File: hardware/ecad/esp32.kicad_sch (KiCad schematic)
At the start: 0 parts

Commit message: finsihed 6/7 sheets, usb_data needs work. Some warnings to be dealt with aswell but no hard errors.
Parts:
- added C10: 10uF, Capacitor_SMD:C_01005_0402Metric, symbol Device:C
- added C11, C12, C13, C9: 100nF, Capacitor_SMD:C_01005_0402Metric, symbol Device:C
- added J3: UART, symbol Connector:Conn_01x06_Pin
- added R10: 100, Resistor_SMD:R_0201_0603Metric, symbol Device:R
- added R7, R8, R9: 10k, Resistor_SMD:R_0201_0603Metric, symbol Device:R
- added SW1, SW2: SW_Push, Button_Switch_SMD:SW_SPST_B3U-1000P, symbol Switch:SW_Push
- added SW3: SW_SPDT, Button_Switch_THT:SW_Slide_SPDT_Angled_CK_OS102011MA1Q, symbol Switch:SW_SPDT
- added U4: ESP32-S3-WROOM-1, RF_Module:ESP32-S3-WROOM-1, symbol RF_Module:ESP32-S3-WROOM-1
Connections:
- new net: R10.2, SW3.2 (B)
- new net BAT_SENSE: U4.4 (IO4)
- new net BOOT_BUTTON: C12.1, J3.6 (Pin_6), R8.2, SW2.1, U4.27 (IO0)
- new net EN: C11.1, J3.5 (Pin_5), R7.2, SW1.1, U4.3 (EN)
- new net GND: C10.2, C11.2, C12.2, C13.1, C9.2, J3.2 (Pin_2), R9.2, SW1.2, SW2.2, U4.1 (GND), U4.40 (GND), U4.41 (GND)
- new net MODE_SEL: C13.2, R10.1, R9.1, U4.38 (IO2)
- new net OLED_CLK: U4.29 (IO36)
- new net OLED_CS: U4.17 (IO9)
- new net OLED_DC: U4.18 (IO10)
- new net OLED_MOSI: U4.28 (IO35)
- new net OLED_RES: U4.12 (IO8)
- new net RX0: J3.4 (Pin_4), U4.36 (RXD0)
- new net SYS_3V3: C10.1, C9.1, J3.1 (Pin_1), R7.1, R8.1, SW3.1 (A), U4.2 (3V3)
- new net TX0: J3.3 (Pin_3), U4.37 (TXD0)
- new net USB_D+_ESP: U4.14 (USB_D+)
- new net USB_D-_ESP: U4.13 (USB_D-)
- no-connect marks 0 -> 25
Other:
- company: (none) -> āvega systems
- title: (none) -> midi2BLE_ESP32_S3

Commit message: Updated schematics to get rid of errors and warnings
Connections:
- net EN renamed RST_BUTTON
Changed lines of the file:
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@@
-	)
-	(junction
-		(at 135.89 63.5)
-		(diameter 0)
-		(color 0 0 0 0)
-	)
-	(junction
-		(at 135.89 68.58)
-		(diameter 0)
-		(color 0 0 0 0)
 	)
 	(junction
@@
 	(wire
 		(pts
-			(xy 132.08 60.96) (xy 135.89 60.96)
+			(xy 132.08 63.5) (xy 135.89 63.5)
 		)
 		(stroke
@@
 	(wire
 		(pts
-			(xy 135.89 68.58) (xy 135.89 66.04)
-		)
-		(stroke
-			(width 0)
-			(type default)
-		)
-	)
-	(wire
-		(pts
 			(xy 208.28 20.32) (xy 215.9 20.32)
 		)
@@
 	(wire
 		(pts
-			(xy 135.89 60.96) (xy 135.89 63.5)
-		)
-		(stroke
-			(width 0)
-			(type default)
-		)
-	)
-	(wire
-		(pts
-			(xy 135.89 66.04) (xy 132.08 66.04)
+			(xy 135.89 68.58) (xy 132.08 68.58)
 		)
 		(stroke
@@
 	(wire
 		(pts
-			(xy 132.08 68.58) (xy 135.89 68.58)
-		)
-		(stroke
-			(width 0)
-			(type default)
-		)
-	)
-	(wire
-		(pts
 			(xy 142.24 166.37) (xy 138.43 166.37)
 		)
@@
 	(wire
 		(pts
-			(xy 132.08 63.5) (xy 135.89 63.5)
-		)
-		(stroke
-			(width 0)
-			(type default)
-		)
-	)
-	(wire
-		(pts
 			(xy 269.24 45.72) (xy 269.24 41.91)
 		)
@@
 		)
 	)
-	(label "IO0"
-		(at 132.08 68.58 180)
-		(effects
-			(font
-				(size 1.27 1.27)
-			)
-			(justify right bottom)
-		)
-	)
-	(label "IO0"
+	(label "BOOT_BUTTON"
 		(at 215.9 33.02 0)
 		(effects
@@
 	)
 	(label "RST_BUTTON"
-		(at 132.08 60.96 180)
+		(at 132.08 63.5 180)
 		(effects
 			(font
@@
 	)
 	(label "BOOT_BUTTON"
-		(at 132.08 66.04 180)
+		(at 132.08 68.58 180)
 		(effects
 			(font
@@
 		)
 	)
-	(label "EN"
-		(at 132.08 63.5 180)
-		(effects
-			(font
-				(size 1.27 1.27)
-			)
-			(justify right bottom)
-		)
-	)
 	(label "RX0"
 		(at 215.9 27.94 0)
@@
 		)
 	)
-	(label "EN"
+	(label "RST_BUTTON"
 		(at 215.9 30.48 0)
 		(effects

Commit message: Updated schematics and added printed pdf
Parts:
- C10: footprint Capacitor_SMD:C_01005_0402Metric -> Capacitor_SMD:C_0603_1608Metric
- C11, C12, C9: footprint Capacitor_SMD:C_01005_0402Metric -> Capacitor_SMD:C_0402_1005Metric
- R10, R7, R8, R9: footprint Resistor_SMD:R_0201_0603Metric -> Capacitor_SMD:C_0402_1005Metric
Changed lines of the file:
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@@
 			)
 		)
-		(property "Footprint" "Capacitor_SMD:C_01005_0402Metric"
+		(property "Footprint" "Capacitor_SMD:C_0402_1005Metric"
 			(at 260.35 61.2648 0)
 			(hide yes)
@@
 			)
 		)
-		(property "Footprint" "Capacitor_SMD:C_01005_0402Metric"
+		(property "Footprint" "Capacitor_SMD:C_0603_1608Metric"
 			(at 260.35 40.9448 0)
 			(hide yes)
@@
 			)
 		)
-		(property "Footprint" "Capacitor_SMD:C_01005_0402Metric"
+		(property "Footprint" "Capacitor_SMD:C_0402_1005Metric"
 			(at 260.35 101.9048 0)
 			(hide yes)
@@
 			)
 		)
-		(property "Footprint" "Resistor_SMD:R_0201_0603Metric"
+		(property "Footprint" "Capacitor_SMD:C_0402_1005Metric"
 			(at 255.27 87.122 90)
 			(hide yes)
@@
 			)
 		)
-		(property "Footprint" "Capacitor_SMD:C_01005_0402Metric"
+		(property "Footprint" "Capacitor_SMD:C_0402_1005Metric"
 			(at 260.35 28.2448 0)
 			(hide yes)
@@
 			)
 		)
-		(property "Footprint" "Resistor_SMD:R_0201_0603Metric"
+		(property "Footprint" "Capacitor_SMD:C_0402_1005Metric"
 			(at 52.07 24.638 90)
 			(hide yes)
@@
 			)
 		)
-		(property "Footprint" "Resistor_SMD:R_0201_0603Metric"
+		(property "Footprint" "Capacitor_SMD:C_0402_1005Metric"
 			(at 29.972 30.48 90)
 			(hide yes)
@@
 			)
 		)
-		(property "Footprint" "Resistor_SMD:R_0201_0603Metric"
+		(property "Footprint" "Capacitor_SMD:C_0402_1005Metric"
 			(at 255.27 127.762 90)
 			(hide yes)

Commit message: docs(hardware): update ecad README to reflect completed schematic and PCB — PCB IS DONE!!!
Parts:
- removed J3: UART, symbol Connector:Conn_01x06_Pin
- added TP1, TP2, TP3, TP4, TP5, TP6: TestPoint, symbol Connector:TestPoint
- C13: footprint Capacitor_SMD:C_01005_0402Metric -> Capacitor_SMD:C_0402_1005Metric
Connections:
- net BOOT_BUTTON: now also TP6.1
- net GND: now also TP2.1
- net RST_BUTTON: now also TP5.1
- net RX0: now also TP4.1
- net SYS_3V3: now also TP1.1
- net TX0: now also TP3.1
- net USB_D+_ESP renamed USB_ESP+
- net USB_D-_ESP renamed USB_ESP-
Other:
- note added: "UART TEST POINTS"

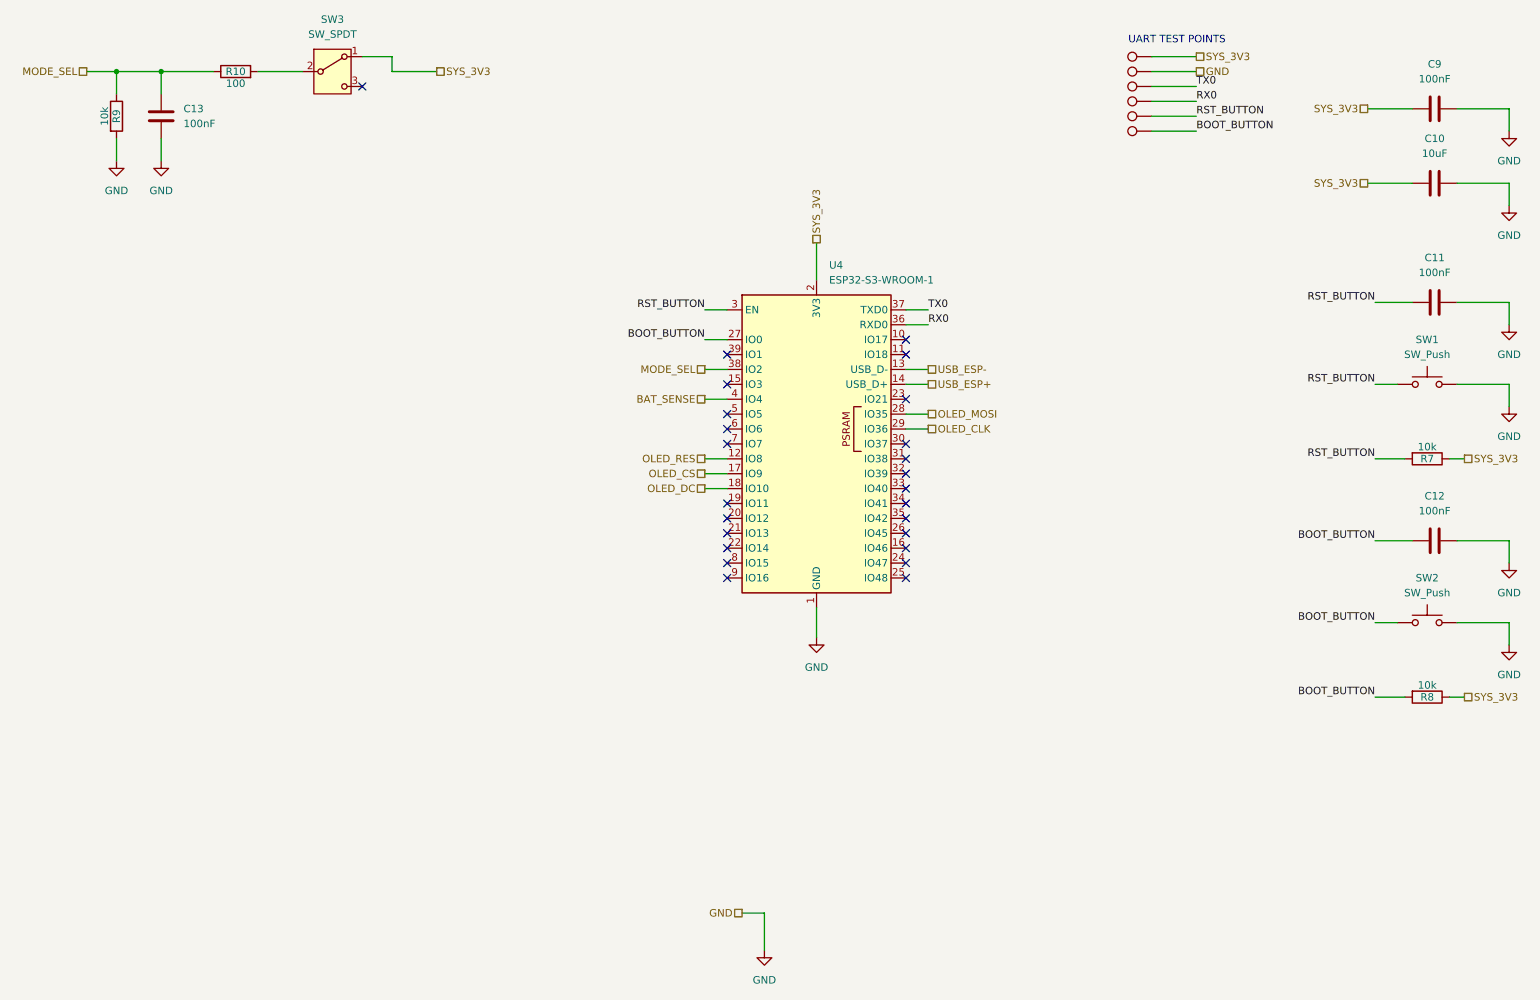
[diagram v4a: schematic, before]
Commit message: fix: resolve fatal power and USB switching errors
Replace TLV61047 boost converter with MT3608; add SS14 catch diode, 4.7µH inductor, and correct FB divider (180kΩ/51kΩ) for 5V output
Fix TPS62162DSG EN circular dependency; connect directly to U1_OUT
Fix TPS62162DSG FB pin; disconnect from SYS_3V3 and tie to GND
Fix TPS2116 power mux; remove series resistor on VIN1, add correct PR1 divider (100kΩ/27kΩ), tie MODE to VIN1 for priority mode
Fix TS3USB30E OE pin; tie directly to GND to keep switch always enabled
Add PGOOD pull-up resistor (10kΩ) to SYS_3V3 on BQ24079
Change ISET resistor from 590Ω to 680Ω for 1.3A charge current
Remove unnecessary R5 (10kΩ VBUS_IN to GND bleed resistor)
Add USB_STATUS net from TPS2116 ST pin to ESP32 IO38
Add PWR_FLAG to BOOST_5V and U1_OUT nets
Fix U1_PGOOD net label placement; separate from SYS_3V3 pull-up node
Add documentation boxes and truth tables to power and USB switching pages
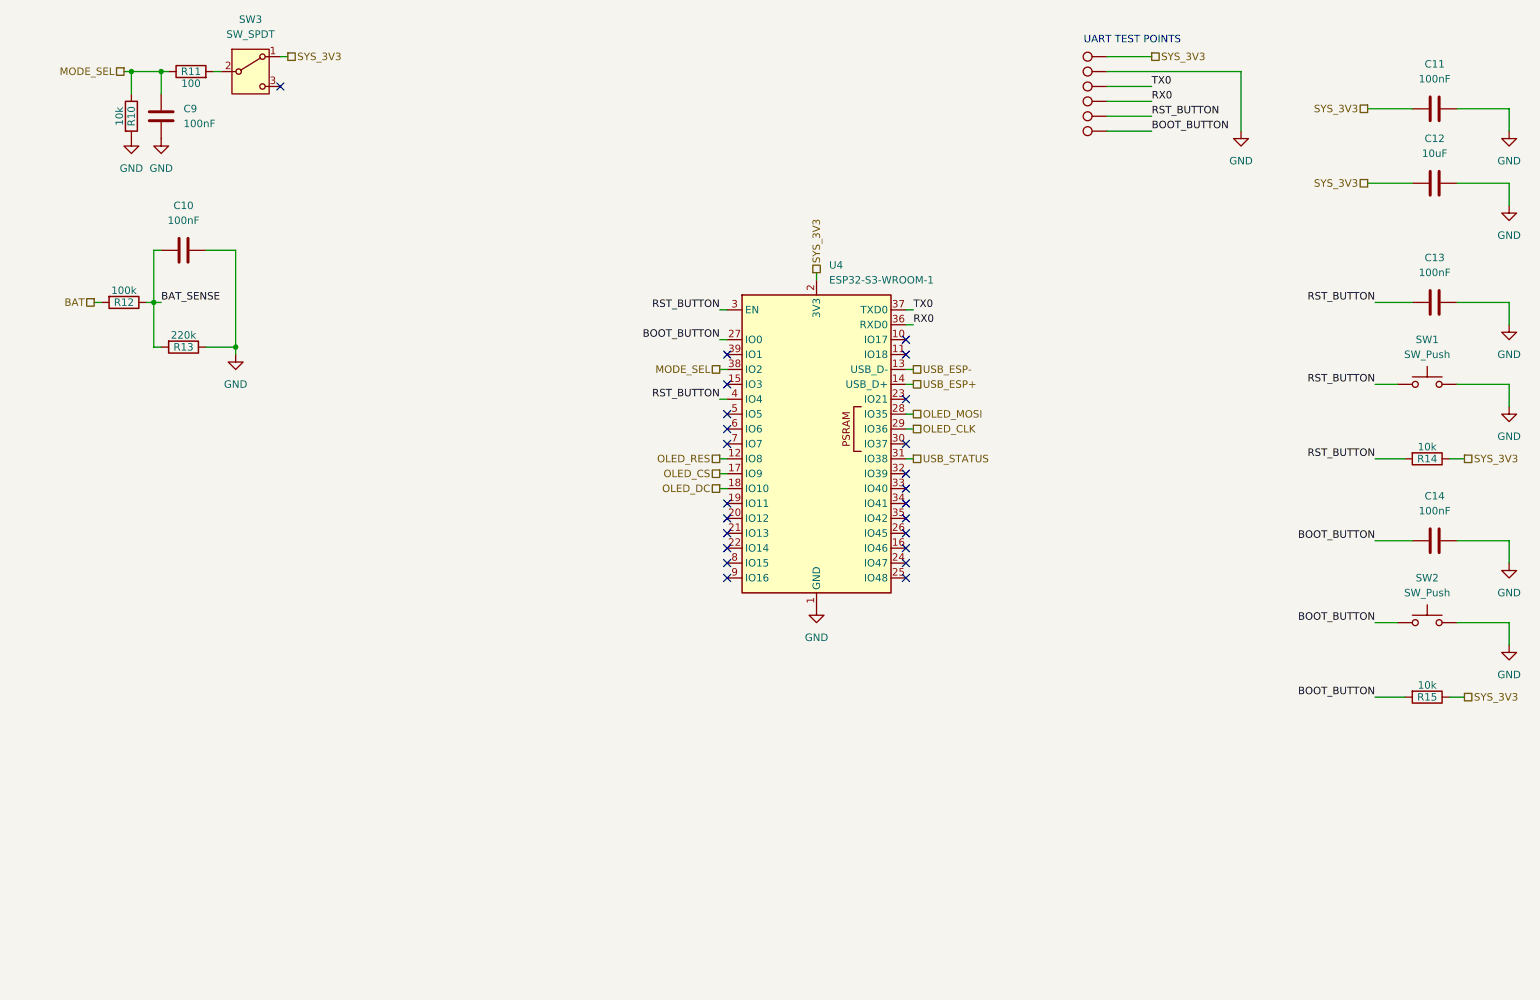
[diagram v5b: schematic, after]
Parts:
- added C10: 100nF, Capacitor_SMD:C_0402_1005Metric, symbol Device:C
- added R12: 100k, Capacitor_SMD:C_0402_1005Metric, symbol Device:R
- added R13: 220k, Capacitor_SMD:C_0402_1005Metric, symbol Device:R
- renumbered C9 to C11, C10 to C12, C11 to C13, C12 to C14, C13 to C9, R9 to R10, R10 to R11, R7 to R14, R8 to R15
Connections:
- net BAT_SENSE: now also C10.1, R12.1, R13.2; no longer U4.4 (IO4)
- net GND: now also C10.2, R13.1
- net RST_BUTTON: now also U4.4 (IO4)
- net USB_STATUS: now reaches U4.31 (IO38)
- new net BAT: R12.2
- no-connect marks 25 -> 24
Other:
- moved on the sheet: R10, R11, SW3

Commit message: Fixed minor errors and smaller issues withing schematics, moved v1 pcb and specific projet artifacts to archive. Produced PDF of full schematic
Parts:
- C10, C11, C13, C14, C9: footprint Capacitor_SMD:C_0402_1005Metric -> Capacitor_SMD:C_0603_1608Metric
- R10, R11, R12, R13, R14, R15: footprint Capacitor_SMD:C_0402_1005Metric -> Resistor_SMD:R_0603_1608Metric
- TP1, TP2, TP3, TP4, TP5, TP6: footprint (none) -> TestPoint:TestPoint_THTPad_D1.0mm_Drill0.5mm
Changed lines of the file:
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@@
 	(title_block
 		(title "midi2BLE_ESP32_S3")
-		(date "2026-04-13")
-		(rev "1")
+		(date "2026-05-16")
+		(rev "2")
 		(company "āvega systems")
 	)
@@
 			)
 		)
-		(property "Footprint" ""
+		(property "Footprint" "TestPoint:TestPoint_THTPad_D1.0mm_Drill0.5mm"
 			(at 200.66 25.4 0)
 			(hide yes)
@@
 			)
 		)
-		(property "Footprint" "Capacitor_SMD:C_0402_1005Metric"
+		(property "Footprint" "Capacitor_SMD:C_0603_1608Metric"
 			(at 260.35 61.2648 0)
 			(hide yes)
@@
 			)
 		)
-		(property "Footprint" "Capacitor_SMD:C_0402_1005Metric"
+		(property "Footprint" "Capacitor_SMD:C_0603_1608Metric"
 			(at 38.4048 26.67 0)
 			(hide yes)
@@
 			)
 		)
-		(property "Footprint" ""
+		(property "Footprint" "TestPoint:TestPoint_THTPad_D1.0mm_Drill0.5mm"
 			(at 200.66 15.24 0)
 			(hide yes)
@@
 			)
 		)
-		(property "Footprint" ""
+		(property "Footprint" "TestPoint:TestPoint_THTPad_D1.0mm_Drill0.5mm"
 			(at 200.66 27.94 0)
 			(hide yes)
@@
 			)
 		)
-		(property "Footprint" ""
+		(property "Footprint" "TestPoint:TestPoint_THTPad_D1.0mm_Drill0.5mm"
 			(at 200.66 17.78 0)
 			(hide yes)
@@
 			)
 		)
-		(property "Footprint" ""
+		(property "Footprint" "TestPoint:TestPoint_THTPad_D1.0mm_Drill0.5mm"
 			(at 200.66 22.86 0)
 			(hide yes)
@@
 			)
 		)
-		(property "Footprint" "Capacitor_SMD:C_0402_1005Metric"
+		(property "Footprint" "Capacitor_SMD:C_0603_1608Metric"
 			(at 260.35 101.9048 0)
 			(hide yes)
@@
 			)
 		)
-		(property "Footprint" "Capacitor_SMD:C_0402_1005Metric"
+		(property "Footprint" "Resistor_SMD:R_0603_1608Metric"
 			(at 255.27 87.122 90)
 			(hide yes)
@@
 			)
 		)
-		(property "Footprint" "Capacitor_SMD:C_0402_1005Metric"
+		(property "Footprint" "Capacitor_SMD:C_0603_1608Metric"
 			(at 260.35 28.2448 0)
 			(hide yes)
@@
 			)
 		)
-		(property "Footprint" "Capacitor_SMD:C_0402_1005Metric"
+		(property "Footprint" "Capacitor_SMD:C_0603_1608Metric"
 			(at 46.99 52.3748 0)
 			(hide yes)
@@
 			)
 		)
-		(property "Footprint" ""
+		(property "Footprint" "TestPoint:TestPoint_THTPad_D1.0mm_Drill0.5mm"
 			(at 200.66 20.32 0)
 			(hide yes)
@@
 			)
 		)
-		(property "Footprint" "Capacitor_SMD:C_0402_1005Metric"
+		(property "Footprint" "Resistor_SMD:R_0603_1608Metric"
 			(at 43.18 68.072 90)
 			(hide yes)
@@
 			)
 		)
-		(property "Footprint" "Capacitor_SMD:C_0402_1005Metric"
+		(property "Footprint" "Resistor_SMD:R_0603_1608Metric"
 			(at 33.02 60.452 90)
 			(hide yes)
@@
 			)
 		)
-		(property "Footprint" "Capacitor_SMD:C_0402_1005Metric"
+		(property "Footprint" "Resistor_SMD:R_0603_1608Metric"
 			(at 44.45 24.638 90)
 			(hide yes)
@@
 			)
 		)
-		(property "Footprint" "Capacitor_SMD:C_0402_1005Metric"
+		(property "Footprint" "Resistor_SMD:R_0603_1608Metric"
 			(at 32.512 30.48 90)
 			(hide yes)
@@
 			)
 		)
-		(property "Footprint" "Capacitor_SMD:C_0402_1005Metric"
+		(property "Footprint" "Resistor_SMD:R_0603_1608Metric"
 			(at 255.27 127.762 90)
 			(hide yes)

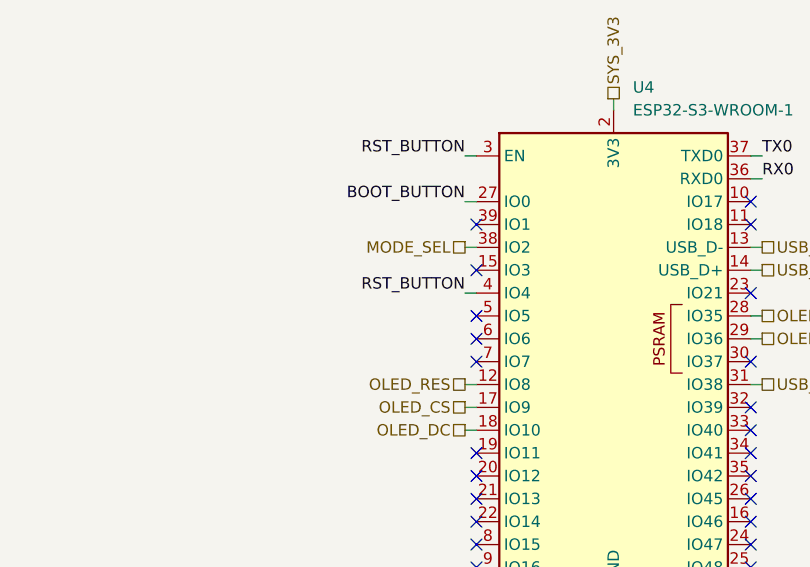
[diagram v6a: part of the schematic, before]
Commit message: Fixed minor errors and smaller issues withing schematics, moved v1 pcb and specific projet artifacts to archive. Updated changelog and finsihed pcb fopr version 2
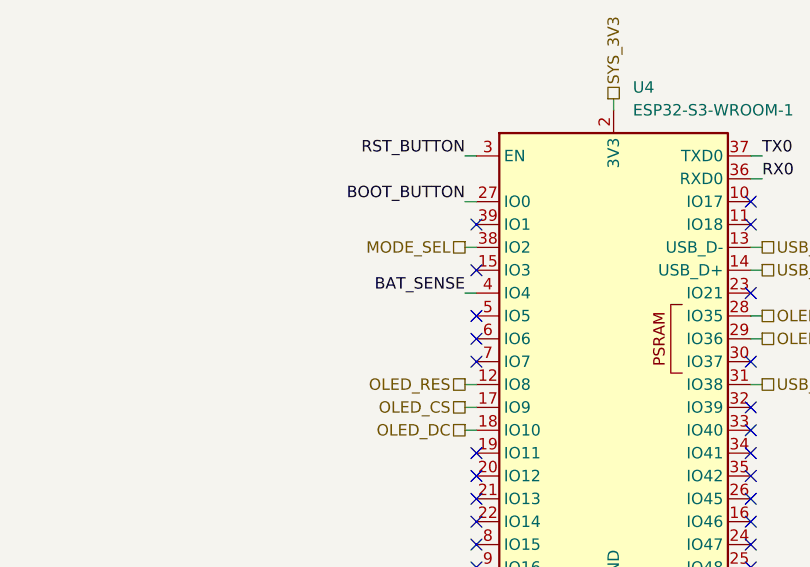
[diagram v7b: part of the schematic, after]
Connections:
- net BAT_SENSE: now also U4.4 (IO4)
- net RST_BUTTON: no longer U4.4 (IO4)
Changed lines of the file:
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@@
-	)
-	(label "RST_BUTTON"
-		(at 134.62 78.74 180)
-		(effects
-			(font
-				(size 1.27 1.27)
-			)
-			(justify right bottom)
-		)
 	)
 	(label "RST_BUTTON"
@@
 		)
 	)
+	(label "BAT_SENSE"
+		(at 134.62 78.74 180)
+		(effects
+			(font
+				(size 1.27 1.27)
+			)
+			(justify right bottom)
+		)
+	)
